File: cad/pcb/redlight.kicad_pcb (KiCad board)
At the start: 2 copper layers, 74.1 x 109.5 mm, 23 parts, among them J1 5V GND VBAT, J2 BUTTON, J3 MAX98357A, SW1 TEST, U1 XIAO ESP32-C6, U2 TBD62083APG

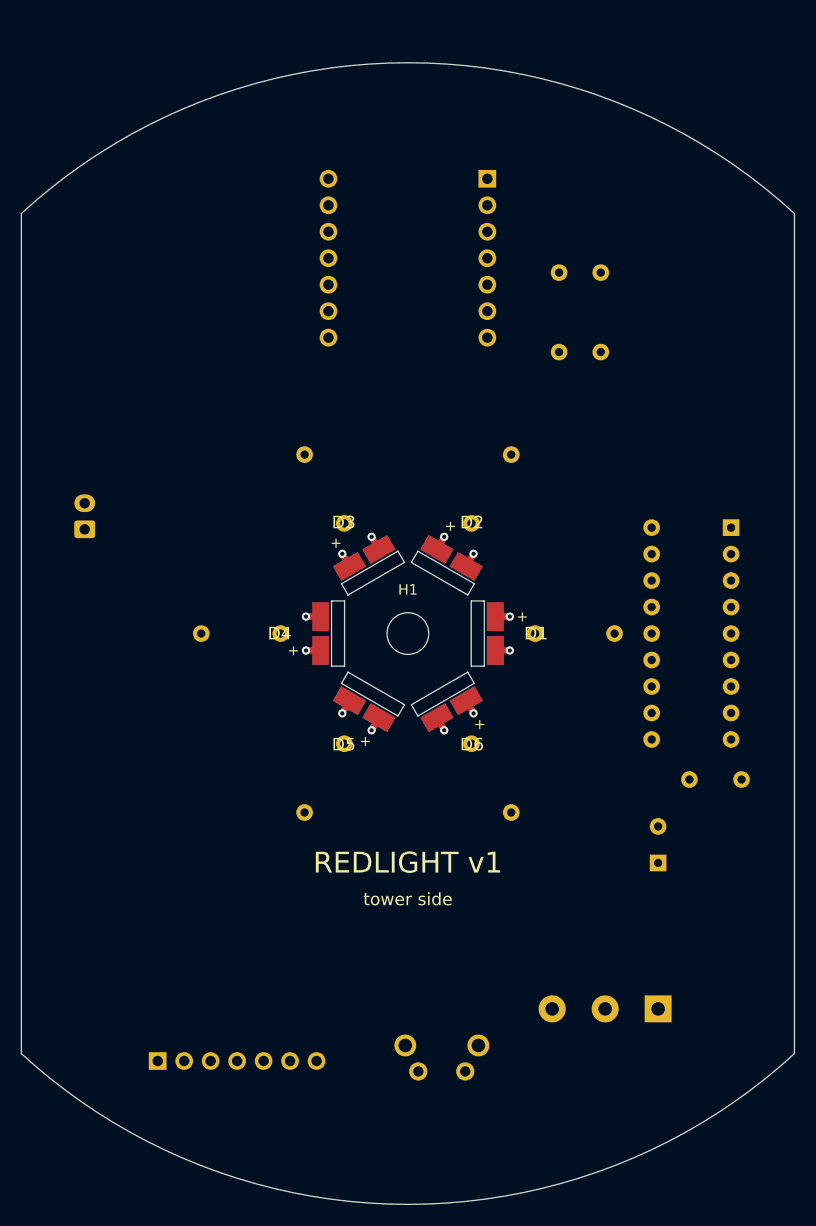
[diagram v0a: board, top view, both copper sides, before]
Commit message: Route the tower PCB and export Gerbers
Freerouting via xvfb, SES imported by our own parser (KiCad 7's importer
is GUI-only), ground pours on both layers with a keepout under the XIAO
antenna, tab pads moved 0.5 mm off the slots for edge clearance. DRC:
no copper errors or unconnected pads, only cosmetic silkscreen overlaps.

Co-Authored-By: Claude Opus 5.5 <noreply@anthropic.com>
Claude-Session: https://claude.ai/code/session_014zeCf4S4BcArxNfoY6CxYX
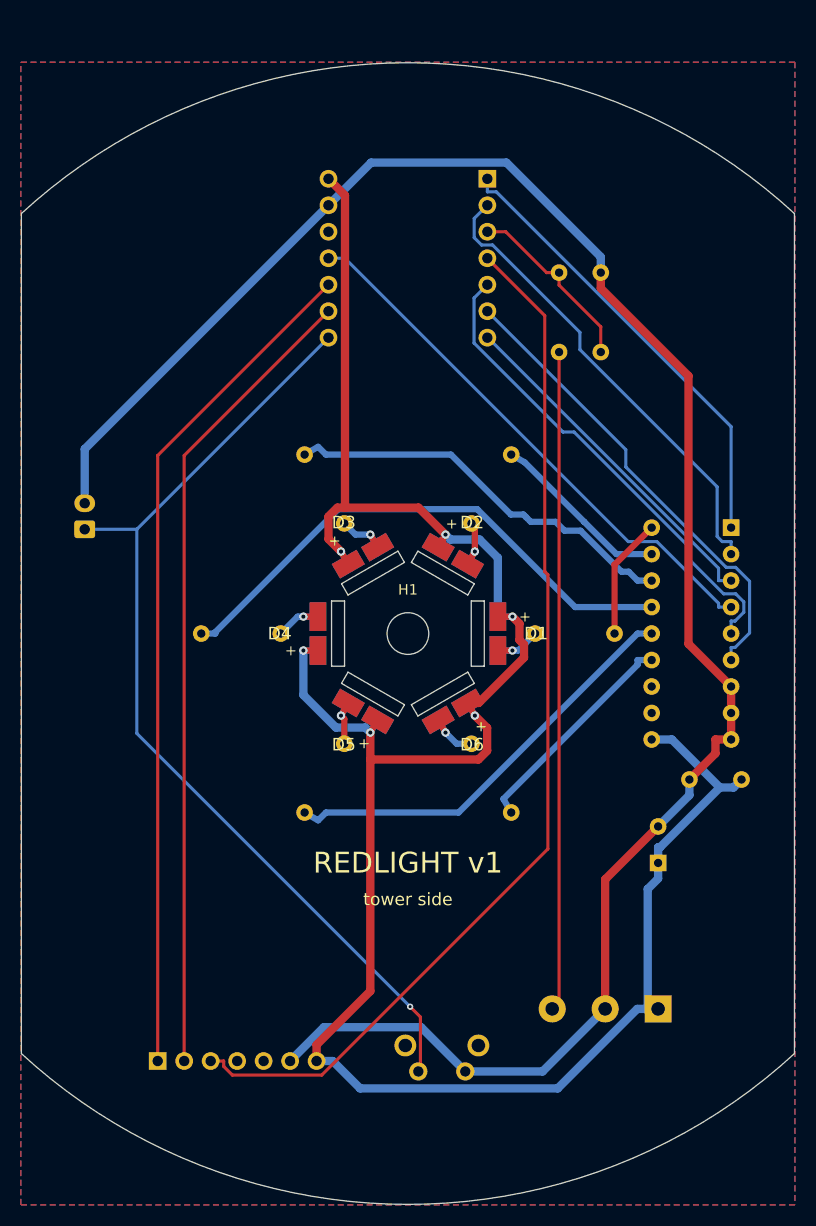
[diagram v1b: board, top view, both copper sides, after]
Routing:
- net +5V: track 16.8 -> 224.1 mm
- net GND: track 0.00 -> 188.8 mm
- net /I2S_DIN: track 0.00 -> 101.3 mm
- net /BUTTON: track 0.00 -> 94.3 mm, vias 0 -> 1
- net /I2S_LRC: track 0.00 -> 81.2 mm
- net /I2S_BCLK: track 0.00 -> 77.7 mm
- net /VBAT: track 0.00 -> 63.3 mm
- net /LIGHT4: track 0.00 -> 52.7 mm
- net /OUT4: track 0.00 -> 52.1 mm
- net /LIGHT5: track 0.00 -> 46.7 mm
- net /LIGHT6: track 0.00 -> 45.4 mm
- net /LIGHT2: track 0.00 -> 45.3 mm
- net /LIGHT1: track 0.00 -> 43.6 mm
- net /OUT5: track 0.00 -> 40.9 mm
- net /OUT3: track 0.00 -> 38.8 mm
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- added copper zone on B.Cu, net GND
- added copper zone on F.Cu, net GND

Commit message: PCB v2: tall parts on tower side, support tab, tighter slots
The speaker sits 11 mm under the board, so the XIAO, driver, amp module
and capacitors move to the (hidden) tower side; the speaker side keeps
only the angled TEST switch and wire solder pads. Add a 17.5 mm support
tab concentric at r+4.3 mm into the housing recess with an optional power
LED, tighten tab slots for the measured 5.15 mm tabs, open the screw hole
to 4.2 mm. Tab pads are now single plated pads, a rule area keeps traces
out from under the tower, and route.py retries until DRC is clean.

Co-Authored-By: Claude Opus 5.5 <noreply@anthropic.com>
Claude-Session: https://claude.ai/code/session_014zeCf4S4BcArxNfoY6CxYX
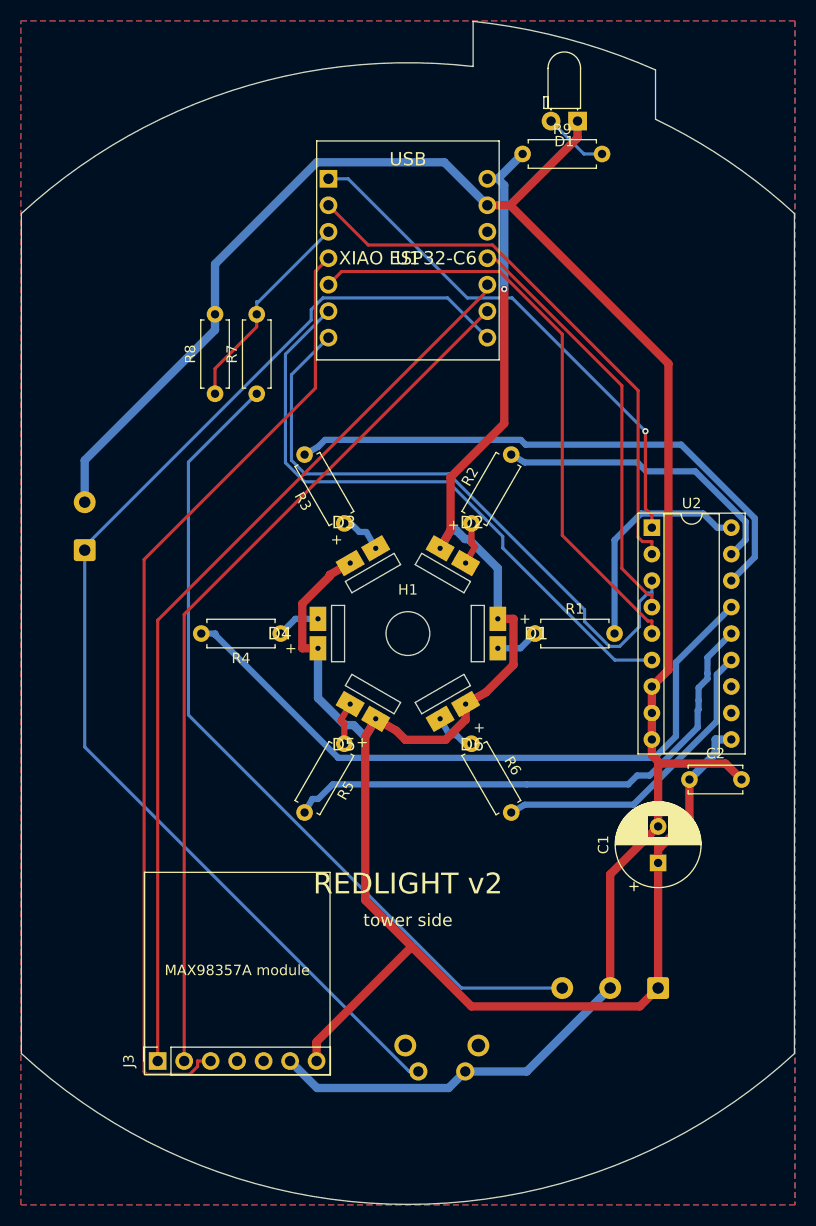
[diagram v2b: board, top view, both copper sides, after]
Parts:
- added D1: power, LED_D3.0mm_Horizontal_O1.27mm_Z2.0mm, F.Cu at (116.3, 50.8)
- added R9: 2k2, R_Axial_DIN0207_L6.3mm_D2.5mm_P7.62mm_Horizontal, F.Cu at (111.0, 54.0)
- C1, C2, J3, R1, R2, R3, R4, R5, R6, R7, R8, U1, U2: moved to F.Cu
- J1: footprint TerminalBlock_Phoenix_MKDS-1,5-3-5.08_1x03_P5.08mm_Horizontal -> SolderWire-0.5sqmm_1x03_P4.6mm_D0.9mm_OD2.1mm
- J2: footprint JST_XH_B2B-XH-A_1x02_P2.50mm_Vertical -> SolderWire-0.5sqmm_1x02_P4.6mm_D0.9mm_OD2.1mm
- moved R8 37.2 mm to (81.5, 77.0)
- moved R7 29.3 mm to (85.5, 77.0)
- moved U2 7.60 mm to (123.4, 89.8), turned to 0 degrees
- moved C2 5.00 mm to (127.0, 114.0), turned to 0 degrees
- moved J1 2.00 mm to (124.0, 134.0)
- moved J2 2.00 mm to (69.0, 92.0)
- turned J3 to 90 degrees
- turned U1 to 0 degrees
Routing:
- net +5V: track 224.1 -> 196.8 mm, vias 6 -> 1
- net /LIGHT3: track 33.7 -> 60.6 mm
- net /BUTTON: track 94.3 -> 114.8 mm, vias 1 -> 0
- net /VBAT: track 63.3 -> 80.2 mm
- net /OUT3: track 38.8 -> 53.7 mm
- net /LIGHT6: track 45.4 -> 59.9 mm
- net /OUT4: track 52.1 -> 66.0 mm
- net GND: track 188.8 -> 201.4 mm
- net /LIGHT4: track 52.7 -> 40.6 mm
- net /OUT2: track 17.3 -> 28.7 mm
- net /LIGHT5: track 46.7 -> 57.9 mm
- net /OUT5: track 40.9 -> 51.6 mm
- net /OUT1: track 11.6 -> 21.8 mm
- net /I2S_DIN: track 101.3 -> 92.7 mm
- net /LIGHT2: track 45.3 -> 53.8 mm
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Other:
- board size 74.1 x 109.5 mm -> 74.1 x 113.5 mm
- board text added: "REDLIGHT v2"
- board text added: "REDLIGHT v2 speaker side"
- board text added: "max 11 mm parts"
- board text removed: "REDLIGHT v1"

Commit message: Add VOL+/VOL- buttons, measured button positions, 5V ring
Place TEST, VOL+ and VOL- angled switches at the measured positions of
the housing's buttons and read all three on one ADC pin through a resistor
ladder (light 1 moves from D0 to D7 on the XIAO C6). Firmware: debounced
ladder decoding, volume +/-10 with a confirmation beep.

PCB: + is the clockwise half of each tab. Pre-route a 5V ring and the
strip-to-resistor traces around the tower, and split tracks at the
T-junctions Freerouting creates so KiCad sees them as connected (the cause
of the intermittent unconnected-pad failures).

Co-Authored-By: Claude Opus 5.5 <noreply@anthropic.com>
Claude-Session: https://claude.ai/code/session_014zeCf4S4BcArxNfoY6CxYX
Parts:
- added R10: 10k, R_Axial_DIN0207_L6.3mm_D2.5mm_P7.62mm_Horizontal, F.Cu at (75.0, 68.0)
- added R11: 2k2, R_Axial_DIN0207_L6.3mm_D2.5mm_P7.62mm_Horizontal, F.Cu at (69.0, 108.0)
- added R12: 6k8, R_Axial_DIN0207_L6.3mm_D2.5mm_P7.62mm_Horizontal, F.Cu at (111.0, 127.0)
- added SW2: VOL+, SW_Tactile_SPST_Angled_PTS645Vx31-2LFS, B.Cu at (87.7, 144.8)
- added SW3: VOL-, SW_Tactile_SPST_Angled_PTS645Vx31-2LFS, B.Cu at (107.8, 144.8)
- J2: value BUTTON -> EXT TEST
- moved SW1 6.43 mm to (97.8, 136.4)
- moved J3 5.00 mm to (76.0, 136.0)
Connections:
- J2 pad 1: /BUTTON -> /BUTTONS
- SW1 pad 1: /BUTTON -> /BUTTONS
- U1 pad 3V3: (no net) -> +3V3
- U1 pad D0: /LIGHT1 -> /BUTTONS
- U1 pad D7: /BUTTON -> /LIGHT1
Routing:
- net /BUTTONS: track 0.00 -> 132.7 mm
- net /BUTTON: track 114.8 -> 0.00 mm
- net /VOL+: track 0.00 -> 45.8 mm
- net +3V3: track 0.00 -> 40.6 mm
- net /LIGHT1: track 49.9 -> 25.8 mm
- net GND: track 201.4 -> 224.0 mm
- net /VOL-: track 0.00 -> 19.2 mm
- net /I2S_DIN: track 92.7 -> 76.7 mm
- net /LIGHT3: track 60.6 -> 44.6 mm, vias 0 -> 1
- net /LIGHT4: track 40.6 -> 53.8 mm
- net /VBAT: track 80.2 -> 91.8 mm
- net /LIGHT6: track 59.9 -> 52.6 mm, vias 0 -> 1
- net /LIGHT5: track 57.9 -> 51.8 mm, vias 0 -> 1
- net /LIGHT2: track 53.8 -> 48.3 mm, vias 0 -> 1
- net /OUT5: track 51.6 -> 56.6 mm
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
